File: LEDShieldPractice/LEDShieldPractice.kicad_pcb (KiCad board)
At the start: 2 copper layers, 40 x 22.5 mm, 11 parts, among them J1 Conn_02x05_Odd_Even, J2 CLOCK_IN, Q1 2N3904

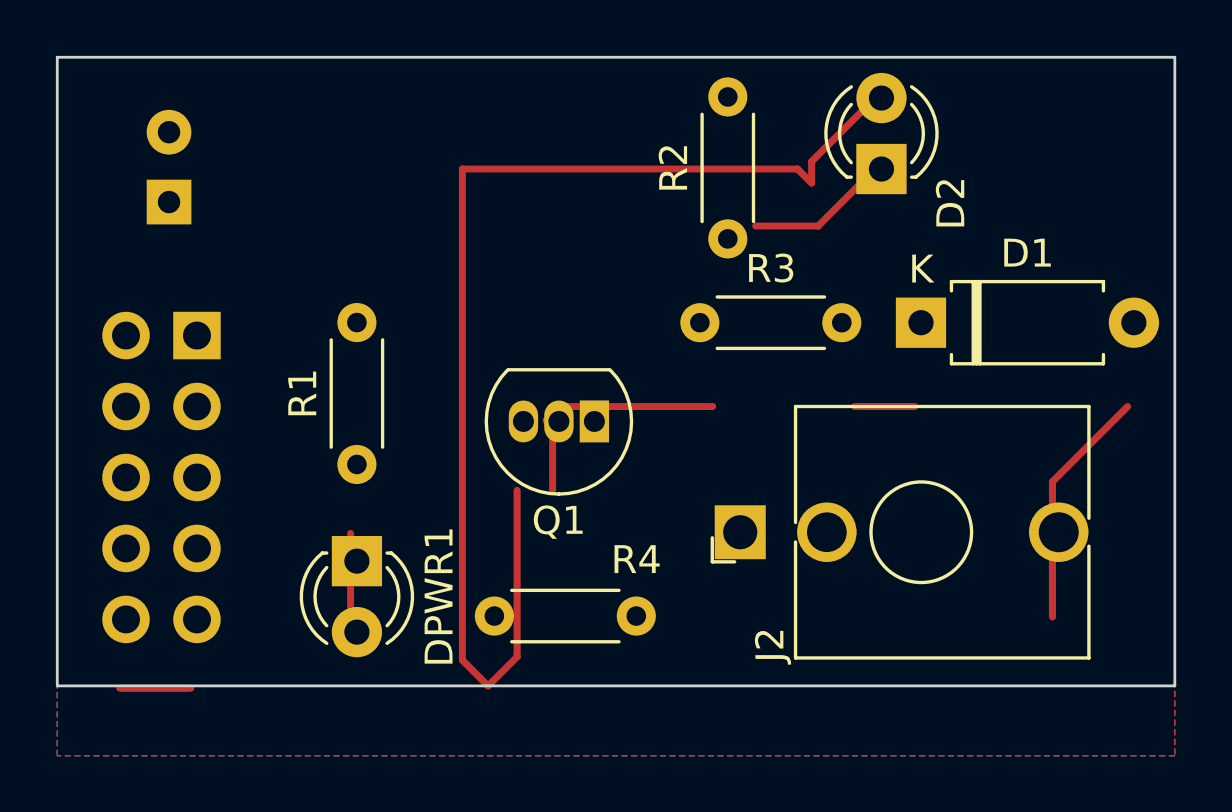
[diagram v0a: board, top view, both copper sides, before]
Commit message: Resize ClockBlink PCB
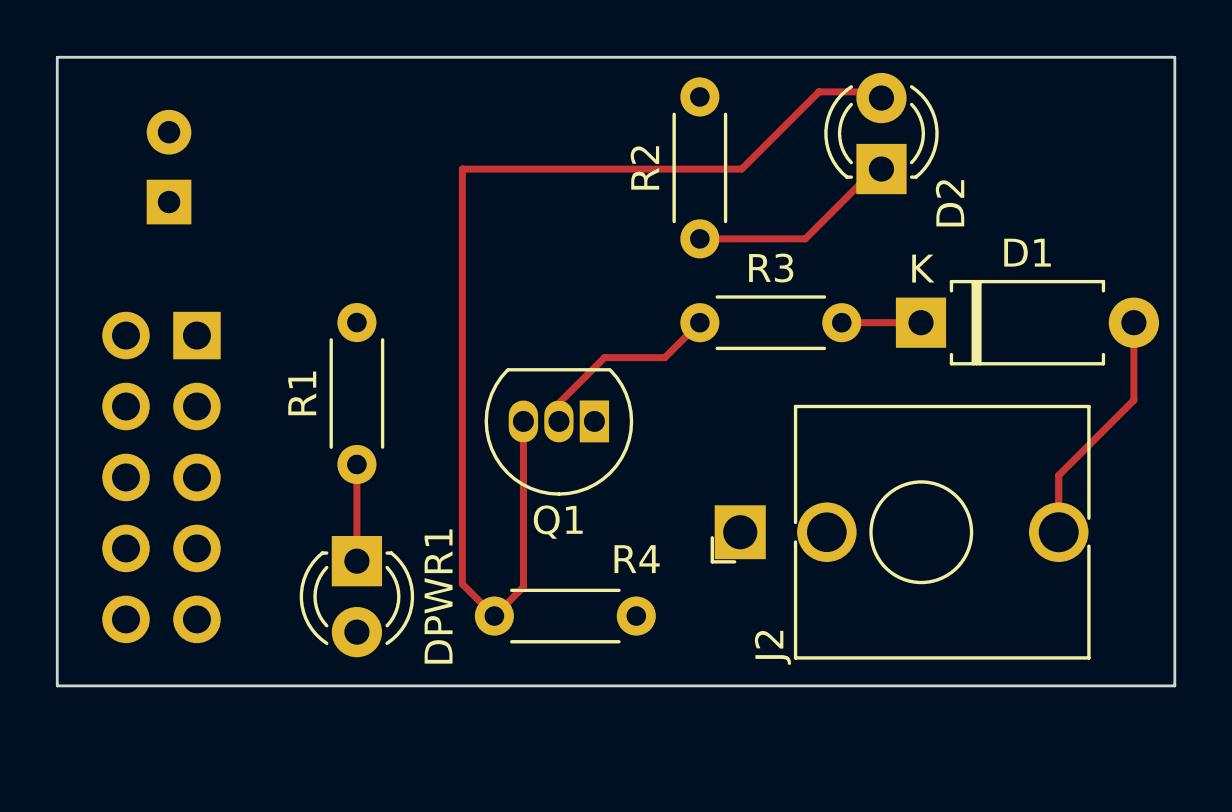
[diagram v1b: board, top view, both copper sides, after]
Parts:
- moved R2 1.00 mm to (47.5, 36.0)
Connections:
- J1 pad 10: /-12V -> unconnected-(J1-Pad10)
- J1 pad 9: /-12V -> unconnected-(J1-Pad9)
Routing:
- net CLOCK: track 43.3 -> 40.0 mm
- net /-12V: track 2.54 -> 0.00 mm
- net Net-(D2-Pad1): track 5.44 -> 7.51 mm
- net Net-(Q1-Pad2): track 8.76 -> 7.18 mm
- net Net-(D1-Pad1): track 2.15 -> 2.84 mm
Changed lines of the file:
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@@
   (net 2 "GND")
   (net 3 "+12V")
-  (net 4 "/-12V")
+  (net 4 "unconnected-(J1-Pad9)")
   (net 5 "Net-(Q1-Pad2)")
   (net 6 "Net-(DPWR1-Pad1)")
@@
   (net 8 "Net-(D1-Pad2)")
   (net 9 "Net-(D2-Pad1)")
+  (net 10 "unconnected-(J1-Pad10)")
   (footprint "Diode_THT:D_A-405_P7.62mm_Horizontal" (layer "F.Cu")
     (at 55.415 39)
@@
   )
   (footprint "Resistor_THT:R_Axial_DIN0204_L3.6mm_D1.6mm_P5.08mm_Horizontal" (layer "F.Cu")
-    (at 48.5 36 90)
+    (at 47.5 36 90)
     (descr "Resistor, Axial_DIN0204 series, Axial, Horizontal, pin pitch=5.08mm, 0.167W, length*diameter=3.6*1.6mm^2, http://cdn-reichelt.de/documents/datenblatt/B400/1_4W%23YAG.pdf")
     (tags "Resistor Axial_DIN0204 series Axial Horizontal pin pitch 5.08mm 0.167W length 3.6mm diameter 1.6mm")
@@
       (effects (font (size 1 1) (thickness 0.15)))
     )
-    (fp_text value "10k" (at 2.54 0) (layer "F.Fab")
+    (fp_text value "10k" (at 2.54 1.75) (layer "F.Fab")
       (effects (font (size 1 1) (thickness 0.15)))
     )
@@
     (property "Sheetname" "")
     (attr through_hole)
-    (fp_text reference "J1" (at 1.27 2.33) (layer "B.SilkS")
+    (fp_text reference "J1" (at -2 2.52738) (layer "B.SilkS")
       (effects (font (size 1 1) (thickness 0.15)) (justify mirror))
     )
@@
       (net 2 "GND") (pinfunction "Pin_8") (pintype "passive"))
     (pad "9" thru_hole oval locked (at 0 -10.16 180) (size 1.7 1.7) (drill 1) (layers *.Cu *.Mask)
-      (net 4 "/-12V") (pinfunction "Pin_9") (pintype "passive+no_connect"))
+      (net 4 "unconnected-(J1-Pad9)") (pinfunction "Pin_9") (pintype "passive+no_connect"))
     (pad "10" thru_hole oval locked (at 2.54 -10.16 180) (size 1.7 1.7) (drill 1) (layers *.Cu *.Mask)
-      (net 4 "/-12V") (pinfunction "Pin_10") (pintype "passive+no_connect"))
+      (net 10 "unconnected-(J1-Pad10)") (pinfunction "Pin_10") (pintype "passive+no_connect"))
     (model "${KICAD6_3DMODEL_DIR}/Connector_PinHeader_2.54mm.3dshapes/PinHeader_2x05_P2.54mm_Vertical.wrl"
       (offset (xyz 0 0 0))
@@
     )
   )
-  (gr_line (start 24.5 49.5) (end 32.5 49.5) (layer "B.SilkS") (width 0.5))
-  (gr_line (start 24.5 52) (end 64.5 52) (layer "Edge.Cuts") (width 0.1))
+  (gr_line (start 25 49.5) (end 33.5 49.5) (layer "B.SilkS") (width 0.5))
+  (gr_line (start 64.5 52) (end 24.5 52) (layer "Edge.Cuts") (width 0.1))
   (gr_line (start 64.5 52) (end 64.5 29.5) (layer "Edge.Cuts") (width 0.1))
   (gr_line locked (start 64.5 29.5) (end 24.5 29.5) (layer "Edge.Cuts") (width 0.1))
   (gr_line (start 24.5 29.5) (end 24.5 52) (layer "Edge.Cuts") (width 0.1))
-  (gr_text "-12V RedStripe" (at 32.225 43.035 90) (layer "B.SilkS")
+  (gr_text "-12V RedStripe" (at 33 43.25 90) (layer "B.SilkS")
     (effects (font (size 1 1) (thickness 0.15)) (justify mirror))
   )
-  (segment (start 55.19 42) (end 53.04 42) (width 0.25) (layer "F.Cu") (net 1))
-  (segment (start 26.735 52.085) (end 29.275 52.085) (width 0.25) (layer "F.Cu") (net 4))
-  (segment (start 42.5 42) (end 42 42.5) (width 0.25) (layer "F.Cu") (net 5))
-  (segment (start 47.96 42) (end 42.5 42) (width 0.25) (layer "F.Cu") (net 5))
-  (segment (start 42.23 42.73) (end 42.23 45) (width 0.25) (layer "F.Cu") (net 5))
-  (segment (start 42 42.5) (end 42.23 42.73) (width 0.25) (layer "F.Cu") (net 5))
-  (segment (start 35 46.54) (end 35 50) (width 0.25) (layer "F.Cu") (net 6))
-  (segment (start 39.92 52) (end 39 51.08) (width 0.25) (layer "F.Cu") (net 7))
-  (segment (start 39 51.08) (end 39 33.5) (width 0.25) (layer "F.Cu") (net 7))
-  (segment (start 39 33.5) (end 51 33.5) (width 0.25) (layer "F.Cu") (net 7))
-  (segment (start 51.5 34) (end 51.5 33.235) (width 0.25) (layer "F.Cu") (net 7))
-  (segment (start 40.96 45) (end 40.96 50.96) (width 0.25) (layer "F.Cu") (net 7))
-  (segment (start 51 33.5) (end 51.5 34) (width 0.25) (layer "F.Cu") (net 7))
-  (segment (start 40.96 50.96) (end 39.92 52) (width 0.25) (layer "F.Cu") (net 7))
-  (segment (start 51.5 33.235) (end 54 30.735) (width 0.25) (layer "F.Cu") (net 7))
-  (segment (start 60.12 49.535241) (end 60.12 44.69) (width 0.25) (layer "F.Cu") (net 8))
-  (segment (start 60.12 44.69) (end 62.81 42) (width 0.25) (layer "F.Cu") (net 8))
-  (segment (start 49.5 35.54) (end 51.735 35.54) (width 0.25) (layer "F.Cu") (net 9))
-  (segment (start 51.735 35.54) (end 54 33.275) (width 0.25) (layer "F.Cu") (net 9))
+  (dimension (type aligned) (layer "Cmts.User")
+    (pts (xy 64.5 29.5) (xy 64.5 52))
+    (height -8)
+    (gr_text "22.5000 mm" (at 71.35 40.75 90) (layer "Cmts.User")
+      (effects (font (size 1 1) (thickness 0.15)))
+    )
+    (format (units 3) (units_format 1) (precision 4))
+    (style (thickness 0.15) (arrow_length 1.27) (text_position_mode 0) (extension_height 0.58642) (extension_offset 0.5) keep_text_aligned)
+  )
+  (dimension (type aligned) (layer "Cmts.User")
+    (pts (xy 24.5 29.5) (xy 64.5 29.5))
+    (height -5)
+    (gr_text "40.0000 mm" (at 44.5 23.35) (layer "Cmts.User")
+      (effects (font (size 1 1) (thickness 0.15)))
+    )
+    (format (units 3) (units_format 1) (precision 4))
+    (style (thickness 0.15) (arrow_length 1.27) (text_position_mode 0) (extension_height 0.58642) (extension_offset 0.5) keep_text_aligned)
+  )
+  (segment (start 55.415 39) (end 52.58 39) (width 0.25) (layer "F.Cu") (net 1))
+  (segment (start 44.085978 40.25) (end 42.23 42.105978) (width 0.25) (layer "F.Cu") (net 5))
+  (segment (start 47.5 39) (end 46.25 40.25) (width 0.25) (layer "F.Cu") (net 5))
+  (segment (start 42.23 42.105978) (end 42.23 42.73) (width 0.25) (layer "F.Cu") (net 5))
+  (segment (start 46.25 40.25) (end 44.085978 40.25) (width 0.25) (layer "F.Cu") (net 5))
+  (segment (start 35.225 47.535) (end 35.225 44.075) (width 0.25) (layer "F.Cu") (net 6))
+  (segment (start 39 48.355) (end 39 33.5) (width 0.25) (layer "F.Cu") (net 7))
+  (segment (start 41.185 48.46) (end 40.145 49.5) (width 0.25) (layer "F.Cu") (net 7))
+  (segment (start 49 33.5) (end 51.765 30.735) (width 0.25) (layer "F.Cu") (net 7))
+  (segment (start 40.145 49.5) (end 39 48.355) (width 0.25) (layer "F.Cu") (net 7))
+  (segment (start 39 33.5) (end 49 33.5) (width 0.25) (layer "F.Cu") (net 7))
+  (segment (start 51.765 30.735) (end 54 30.735) (width 0.25) (layer "F.Cu") (net 7))
+  (segment (start 41.185 42.535) (end 41.185 48.46) (width 0.25) (layer "F.Cu") (net 7))
+  (segment (start 63.035 41.775) (end 63.035 39) (width 0.25) (layer "F.Cu") (net 8))
+  (segment (start 60.345 44.465) (end 63.035 41.775) (width 0.25) (layer "F.Cu") (net 8))
+  (segment (start 60.345 46.5) (end 60.345 44.465) (width 0.25) (layer "F.Cu") (net 8))
+  (segment (start 47.5 36) (end 51.25 36) (width 0.25) (layer "F.Cu") (net 9))
+  (segment (start 53.775 33.5) (end 54 33.5) (width 0.25) (layer "F.Cu") (net 9))
+  (segment (start 51.275 36) (end 53.775 33.5) (width 0.25) (layer "F.Cu") (net 9))
   (zone (net 3) (net_name "+12V") (layer "F.Cu") (hatch edge 0.508)
     (connect_pads (clearance 0.508))
@@
       (pts
         (xy 64.5 29.5)
-        (xy 64.5 54.5)
-        (xy 24.5 54.5)
+        (xy 64.5 52)
+        (xy 24.5 52)
         (xy 24.5 29.5)
       )
@@
       (pts
         (xy 64.5 29.5)
-        (xy 64.5 54.5)
-        (xy 24.5 54.5)
+        (xy 64.5 52)
+        (xy 24.5 52)
         (xy 24.5 29.5)
       )

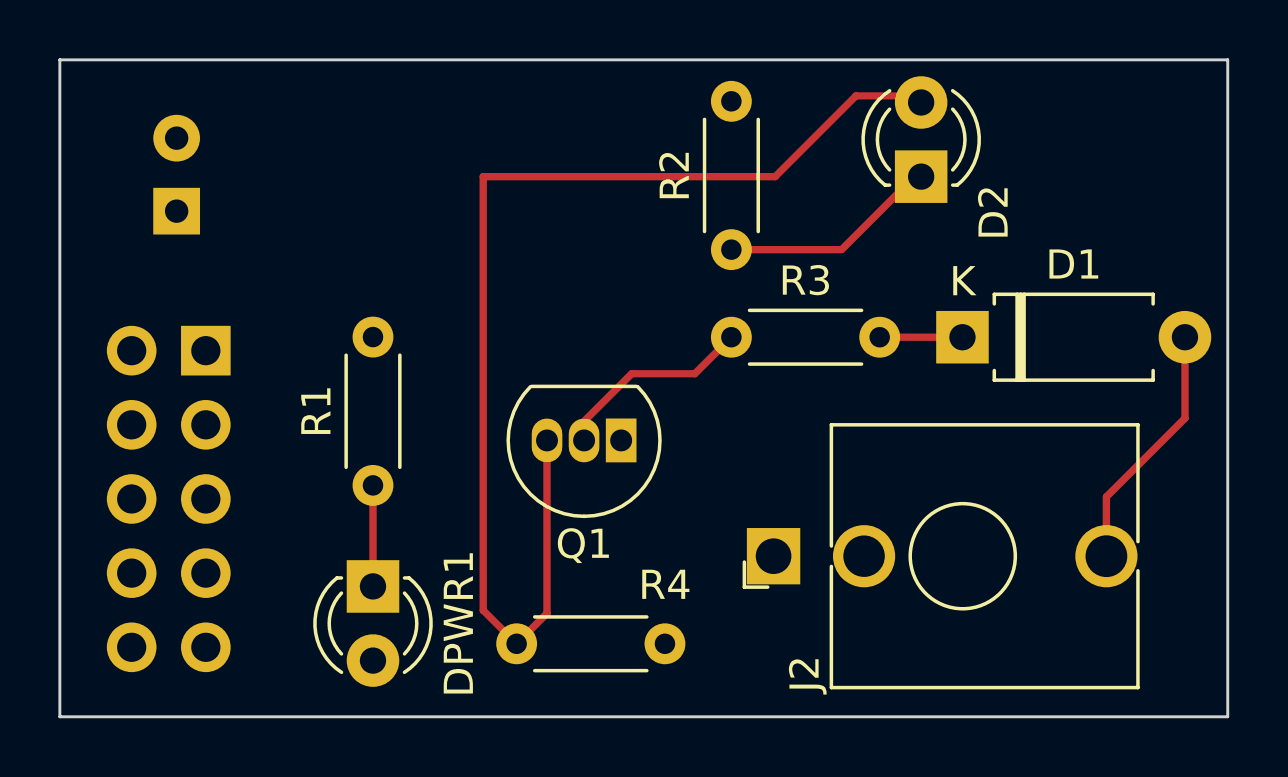
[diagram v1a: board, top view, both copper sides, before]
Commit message: Update LED Shield Practice
Updated footprints for flush fitting resistors and reran traces. Build 2nd board from last years run, changed led resistors from 500 to 2k, 500 burned out leds with 12v.
Board works but the clock led is lit and turns off when it receives a signal, the transistor is acting as a logic NOT, unsure how to debug, need time on the breadboard.
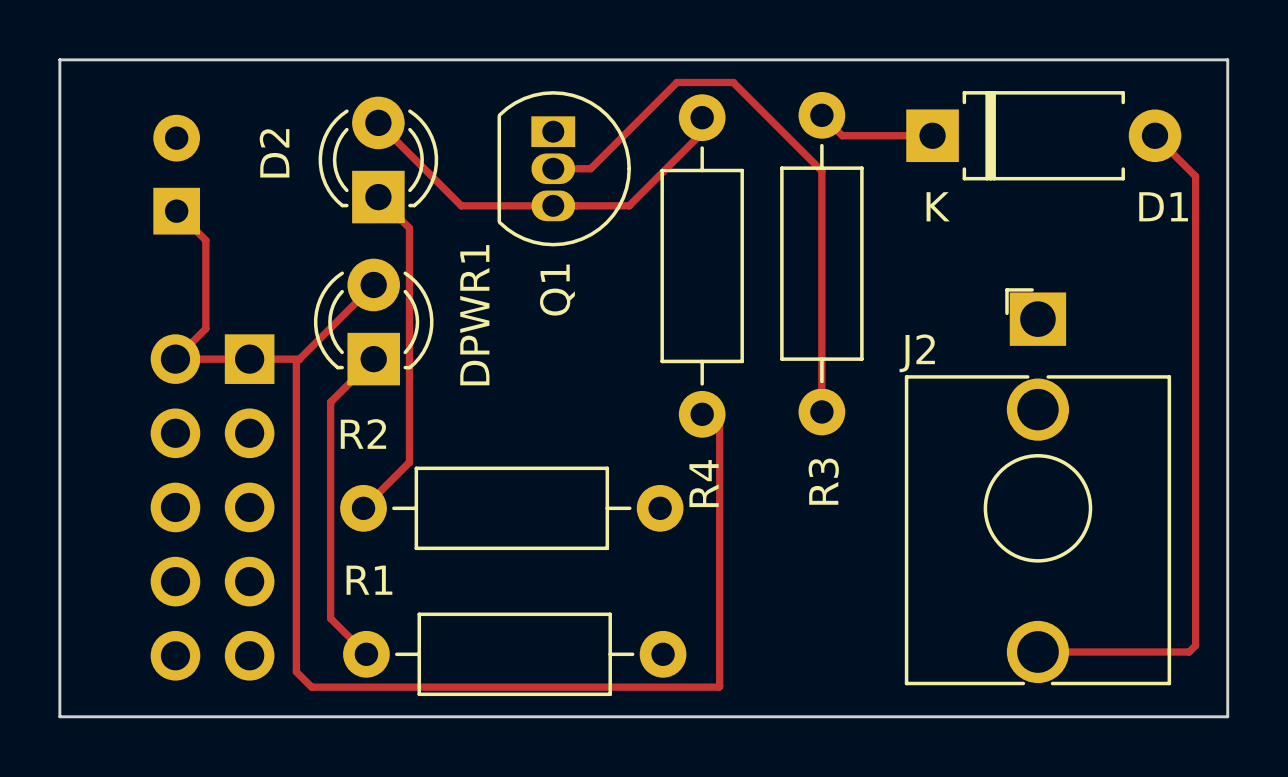
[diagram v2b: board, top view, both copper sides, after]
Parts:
- R1, R2: value 500 -> 2000; footprint Resistor_THT:R_Axial_DIN0204_L3.6mm_D1.6mm_P5.08mm_Horizontal -> Resistor_THT:R_Axial_DIN0207_L6.3mm_D2.5mm_P10.16mm_Horizontal
- R3, R4: footprint Resistor_THT:R_Axial_DIN0204_L3.6mm_D1.6mm_P5.08mm_Horizontal -> Resistor_THT:R_Axial_DIN0207_L6.3mm_D2.5mm_P10.16mm_Horizontal
- moved D2 18.6 mm to (35.4, 34.2)
- moved R2 15.4 mm to (34.9, 44.9), turned to 0 degrees
- moved J2 12.2 mm to (58.0, 38.4), turned to 0 degrees
- moved Q1 10.8 mm to (41.4, 32.0), turned to -90 degrees
- moved R4 7.96 mm to (46.5, 41.6), turned to 90 degrees
- moved DPWR1 7.79 mm to (35.2, 39.8), turned to 90 degrees
- moved D1 6.98 mm to (54.4, 32.1)
- moved R1 5.79 mm to (35.0, 49.9), turned to 0 degrees
- moved R3 4.02 mm to (50.6, 41.6), turned to 90 degrees
- moved J1 1.53 mm to (31.0, 39.8)
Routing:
- net +12V: track 0.00 -> 48.6 mm
- net CLOCK: track 40.0 -> 14.2 mm
- net Net-(D1-Pad2): track 8.61 -> 23.5 mm
- net Net-(Q1-Pad2): track 7.18 -> 19.1 mm
- net Net-(DPWR1-Pad1): track 3.46 -> 11.2 mm
- net Net-(D2-Pad1): track 7.51 -> 11.8 mm
- net Net-(D1-Pad1): track 2.84 -> 4.08 mm
- removed copper zone on F.Cu, net +12V
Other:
- board text added: "+12V"
- board text added: "-12V"
- board text removed: "-12V RedStripe"
